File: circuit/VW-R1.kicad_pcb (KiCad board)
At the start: 2 copper layers, 45.7 x 71.1 mm, 22 parts, among them J1 PIC16F1938, P1 PICkit3, P2 CONN_02X05, SW1 reset

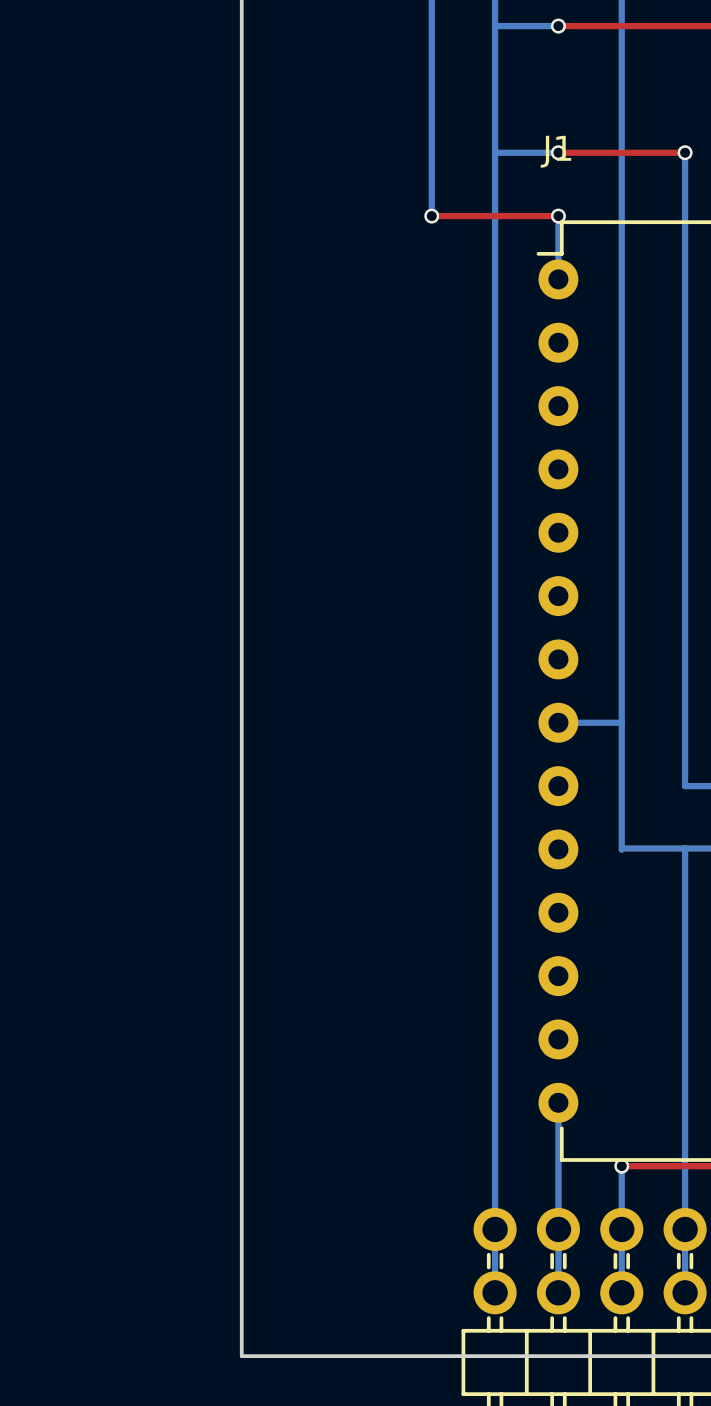
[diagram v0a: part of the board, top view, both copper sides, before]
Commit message: [add] いろいろできるようにコネクタを追加
5ピンコネクタx2.
	・5V/RA3/RA4/RA5/GND
	・5V/RC0/RC1/RC2/GND
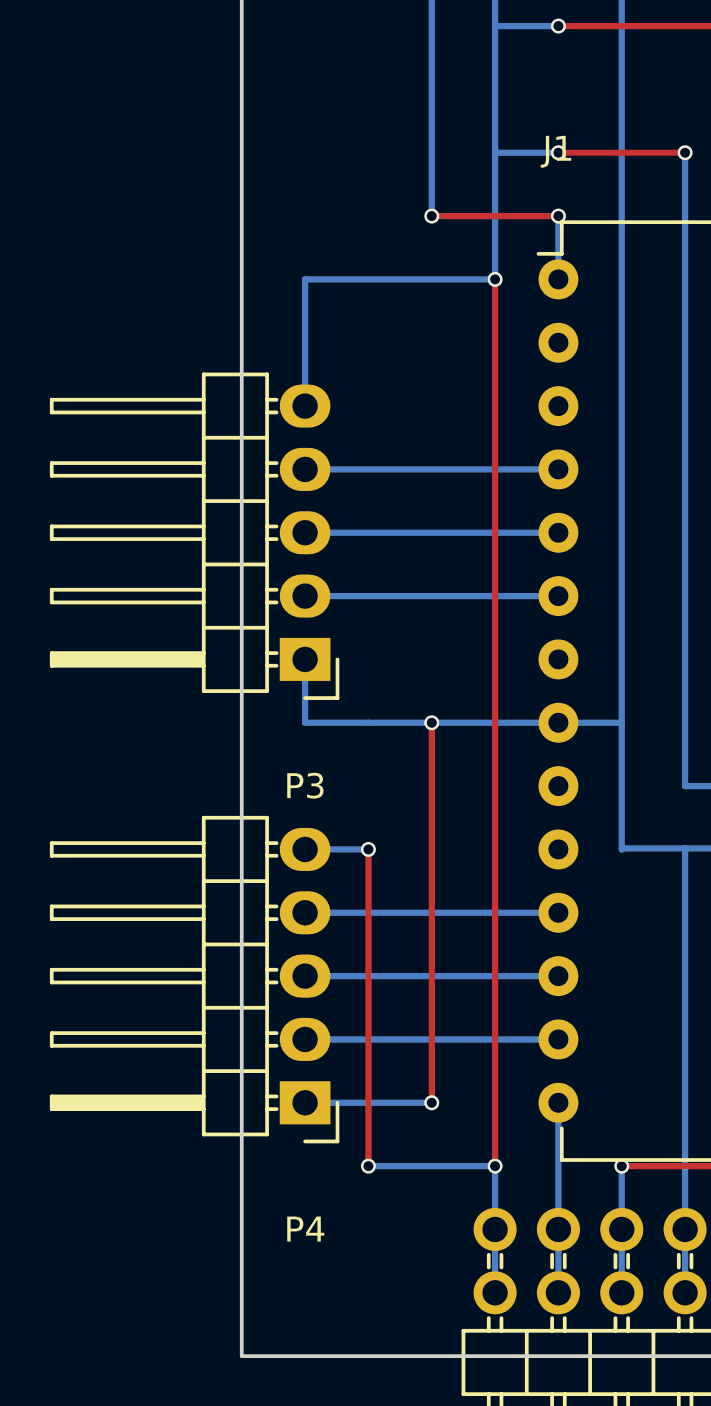
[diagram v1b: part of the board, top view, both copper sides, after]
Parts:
- added P3: CONN_01X05, Pin_Headers:Pin_Header_Angled_1x05, F.Cu at (129.5, 114.3)
- added P4: CONN_01X05, Pin_Headers:Pin_Header_Angled_1x05, F.Cu at (129.5, 132.1)
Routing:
- net GND: track 71.2 -> 104.2 mm, vias 0 -> 2
- net +5V: track 200.7 -> 233.7 mm, vias 4 -> 8
- net Net-(J1-Pad6): track 0.00 -> 10.2 mm
- net Net-(J1-Pad5): track 0.00 -> 10.2 mm
- net Net-(J1-Pad4): track 0.00 -> 10.2 mm
- net Net-(J1-Pad13): track 0.00 -> 10.2 mm
- net Net-(J1-Pad12): track 0.00 -> 10.2 mm
- net Net-(J1-Pad11): track 0.00 -> 10.2 mm

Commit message: [fix] コネクタ周りの配線を修正
追加したコネクタにNHなどの大きめのものを使うと部品と配線が干渉してしまう設計ミスを修正
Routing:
- net +5V: track 233.7 -> 221.0 mm
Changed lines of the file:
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@@
   (general
     (links 58)
-    (no_connects 23)
-    (area 126.924999 71.044999 172.795001 142.315001)
+    (no_connects 13)
+    (area 118.664999 62.784999 172.795001 150.585001)
     (thickness 1.6)
     (drawings 4)
-    (tracks 118)
+    (tracks 119)
     (zones 0)
     (modules 24)
@@
     (pad_to_mask_clearance 0.2)
     (aux_axis_origin 0 0)
-    (visible_elements 7FFFEFFF)
+    (visible_elements 7FFFFFFF)
     (pcbplotparams
       (layerselection 0x00030_80000001)
@@
   (gr_line (start 172.72 71.12) (end 172.72 142.24) (layer Edge.Cuts) (width 0.15))
   (gr_line (start 127 71.12) (end 172.72 71.12) (layer Edge.Cuts) (width 0.15))
-  (segment (start 132.08 134.62) (end 137.16 134.62) (width 0.25) (layer B.Cu) (net 1))
-  (via (at 132.08 134.62) (size 0.6) (drill 0.4) (layers F.Cu B.Cu) (net 1))
-  (segment (start 132.08 121.92) (end 132.08 134.62) (width 0.25) (layer F.Cu) (net 1))
-  (segment (start 129.54 121.92) (end 132.08 121.92) (width 0.25) (layer B.Cu) (net 1))
-  (via (at 132.08 121.92) (size 0.6) (drill 0.4) (layers F.Cu B.Cu) (net 1))
-  (segment (start 137.16 134.62) (end 137.16 99.06) (width 0.25) (layer F.Cu) (net 1))
-  (via (at 137.16 134.62) (size 0.6) (drill 0.4) (layers F.Cu B.Cu) (net 1))
+  (segment (start 137.16 121.92) (end 137.16 119.38) (width 0.25) (layer B.Cu) (net 1))
+  (via (at 137.16 119.38) (size 0.6) (drill 0.4) (layers F.Cu B.Cu) (net 1))
+  (segment (start 129.54 121.92) (end 137.16 121.92) (width 0.25) (layer B.Cu) (net 1))
+  (segment (start 137.16 119.38) (end 137.16 99.06) (width 0.25) (layer F.Cu) (net 1))
+  (segment (start 137.16 132.08) (end 137.16 121.92) (width 0.25) (layer F.Cu) (net 1))
+  (via (at 137.16 121.92) (size 0.6) (drill 0.4) (layers F.Cu B.Cu) (net 1))
+  (segment (start 137.16 134.62) (end 137.16 132.08) (width 0.25) (layer B.Cu) (net 1))
+  (via (at 137.16 132.08) (size 0.6) (drill 0.4) (layers F.Cu B.Cu) (net 1))
   (segment (start 129.54 99.06) (end 129.54 104.14) (width 0.25) (layer B.Cu) (net 1))
   (segment (start 137.16 99.06) (end 129.54 99.06) (width 0.25) (layer B.Cu) (net 1))
@@
   (via (at 139.7 93.98) (size 0.6) (drill 0.4) (layers F.Cu B.Cu) (net 1))
   (segment (start 137.16 137.16) (end 137.16 139.7) (width 0.25) (layer B.Cu) (net 1))
-  (segment (start 132.08 116.84) (end 134.62 116.84) (width 0.25) (layer B.Cu) (net 2))
-  (segment (start 134.62 116.84) (end 139.7 116.84) (width 0.25) (layer B.Cu) (net 2))
   (segment (start 134.62 132.08) (end 134.62 116.84) (width 0.25) (layer F.Cu) (net 2))
   (via (at 134.62 116.84) (size 0.6) (drill 0.4) (layers F.Cu B.Cu) (net 2))
   (segment (start 129.54 132.08) (end 134.62 132.08) (width 0.25) (layer B.Cu) (net 2))
   (via (at 134.62 132.08) (size 0.6) (drill 0.4) (layers F.Cu B.Cu) (net 2))
+  (segment (start 132.08 116.84) (end 134.62 116.84) (width 0.25) (layer B.Cu) (net 2))
+  (segment (start 134.62 116.84) (end 139.7 116.84) (width 0.25) (layer B.Cu) (net 2))
   (segment (start 129.54 116.84) (end 132.08 116.84) (width 0.25) (layer B.Cu) (net 2))
   (segment (start 129.54 114.3) (end 129.54 116.84) (width 0.25) (layer B.Cu) (net 2))
